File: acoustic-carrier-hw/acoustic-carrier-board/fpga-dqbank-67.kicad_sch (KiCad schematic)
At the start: 8 parts, among them IC1 ECP5-BGA256

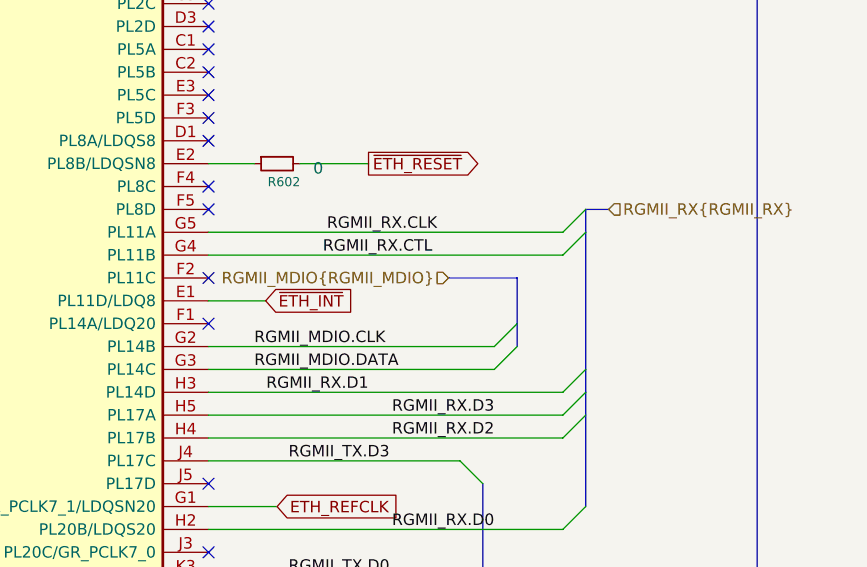
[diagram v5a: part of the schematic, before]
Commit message: [carrier] rerouted USB ULP traces (next) add power planes
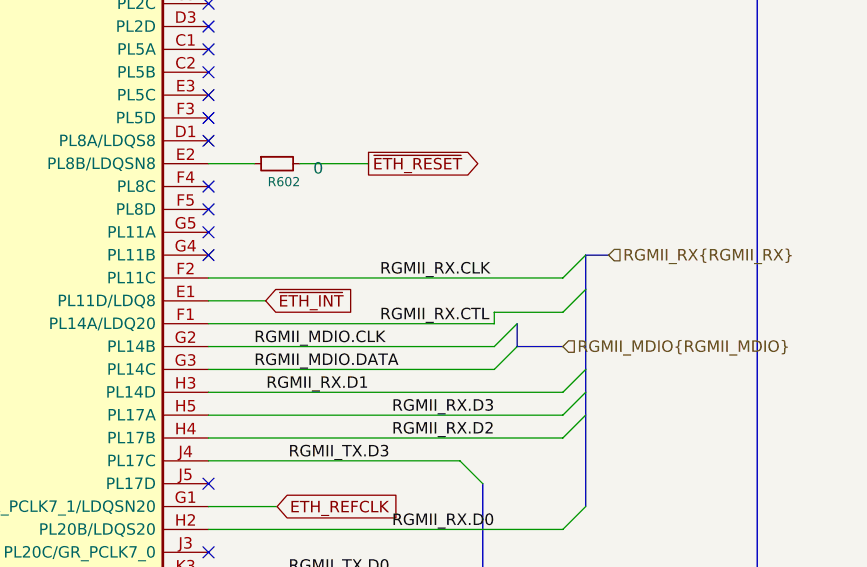
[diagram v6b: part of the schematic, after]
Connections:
- net RGMII_RX.CLK: now also IC1.F2 (PL11C); no longer IC1.G5 (PL11A)
- net RGMII_RX.CTL: now also IC1.F1 (PL14A/LDQ20); no longer IC1.G4 (PL11B)
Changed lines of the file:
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@@
+	)
+	(no_connect
+		(at 220.98 93.98)
 	)
 	(no_connect
@@
 	)
 	(no_connect
-		(at 220.98 99.06)
-	)
-	(no_connect
 		(at 220.98 76.2)
 	)
@@
 	)
 	(no_connect
-		(at 220.98 104.14)
+		(at 220.98 96.52)
 	)
 	(no_connect
@@
 	)
 	(bus_entry
-		(at 262.89 93.98)
+		(at 262.89 100.33)
 		(size -2.54 2.54)
 		(stroke
@@
 	)
 	(bus_entry
-		(at 262.89 91.44)
+		(at 262.89 96.52)
 		(size -2.54 2.54)
 		(stroke
@@
 	(bus
 		(pts
-			(xy 247.65 99.06) (xy 255.27 99.06)
+			(xy 260.35 106.68) (xy 255.27 106.68)
 		)
 		(stroke
@@
 	(wire
 		(pts
+			(xy 252.73 104.14) (xy 252.73 102.87)
+		)
+		(stroke
+			(width 0)
+			(type default)
+		)
+	)
+	(wire
+		(pts
 			(xy 57.15 135.89) (xy 80.01 135.89)
 		)
@@
 	(bus
 		(pts
-			(xy 262.89 91.44) (xy 262.89 93.98)
+			(xy 262.89 96.52) (xy 262.89 100.33)
 		)
 		(stroke
@@
 		)
 	)
-	(wire
-		(pts
-			(xy 220.98 93.98) (xy 260.35 93.98)
-		)
-		(stroke
-			(width 0)
-			(type default)
-		)
-	)
 	(bus
 		(pts
@@
 	(wire
 		(pts
+			(xy 220.98 99.06) (xy 260.35 99.06)
+		)
+		(stroke
+			(width 0)
+			(type default)
+		)
+	)
+	(wire
+		(pts
 			(xy 247.65 45.72) (xy 254 45.72)
 		)
@@
 	(wire
 		(pts
+			(xy 252.73 102.87) (xy 260.35 102.87)
+		)
+		(stroke
+			(width 0)
+			(type default)
+		)
+	)
+	(wire
+		(pts
 			(xy 57.15 64.77) (xy 73.66 64.77)
 		)
@@
 	(bus
 		(pts
-			(xy 265.43 91.44) (xy 262.89 91.44)
-		)
-		(stroke
-			(width 0)
-			(type default)
-		)
-	)
-	(wire
-		(pts
-			(xy 220.98 96.52) (xy 260.35 96.52)
+			(xy 262.89 96.52) (xy 265.43 96.52)
 		)
 		(stroke
@@
 	(bus
 		(pts
-			(xy 262.89 93.98) (xy 262.89 109.22)
+			(xy 262.89 100.33) (xy 262.89 109.22)
 		)
 		(stroke
@@
 		)
 	)
+	(wire
+		(pts
+			(xy 220.98 104.14) (xy 252.73 104.14)
+		)
+		(stroke
+			(width 0)
+			(type default)
+		)
+	)
 	(bus
 		(pts
@@
 		(pts
 			(xy 31.75 50.8) (xy 31.75 54.61)
-		)
-		(stroke
-			(width 0)
-			(type default)
-		)
-	)
-	(bus
-		(pts
-			(xy 255.27 99.06) (xy 255.27 104.14)
 		)
 		(stroke
@@
 	)
 	(label "RGMII_RX.CTL"
-		(at 233.68 96.52 0)
+		(at 240.03 104.14 0)
 		(effects
 			(font
@@
 	)
 	(label "RGMII_RX.CLK"
-		(at 246.38 93.98 180)
-		(effects
-			(font
-				(size 1.27 1.27)
-			)
-			(justify right bottom)
+		(at 240.03 99.06 0)
+		(effects
+			(font
+				(size 1.27 1.27)
+			)
+			(justify left bottom)
 		)
 	)
@@
 	(hierarchical_label "RGMII_MDIO{RGMII_MDIO}"
 		(shape input)
-		(at 247.65 99.06 180)
-		(effects
-			(font
-				(size 1.27 1.27)
-			)
-			(justify right)
+		(at 260.35 106.68 0)
+		(effects
+			(font
+				(size 1.27 1.27)
+			)
+			(justify left)
 		)
 	)
 	(hierarchical_label "RGMII_RX{RGMII_RX}"
 		(shape input)
-		(at 265.43 91.44 0)
-		(effects
-			(font
+		(at 265.43 96.52 0)
+		(effects
+			(font
